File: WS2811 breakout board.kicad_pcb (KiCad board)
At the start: 2 copper layers, 25.4 x 17.8 mm, 15 parts

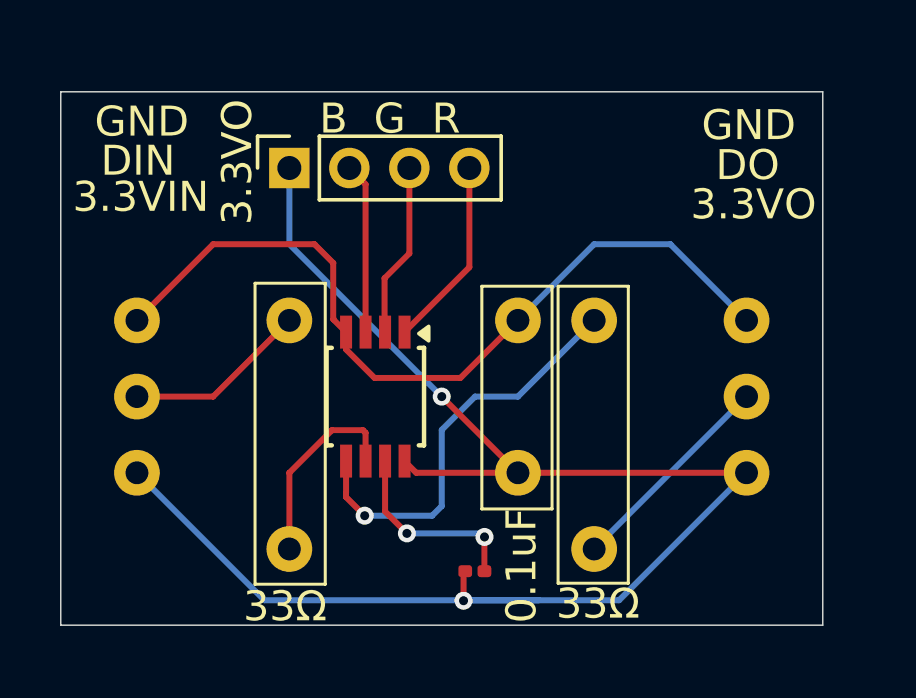
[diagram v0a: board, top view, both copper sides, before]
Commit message: fix sizing issues
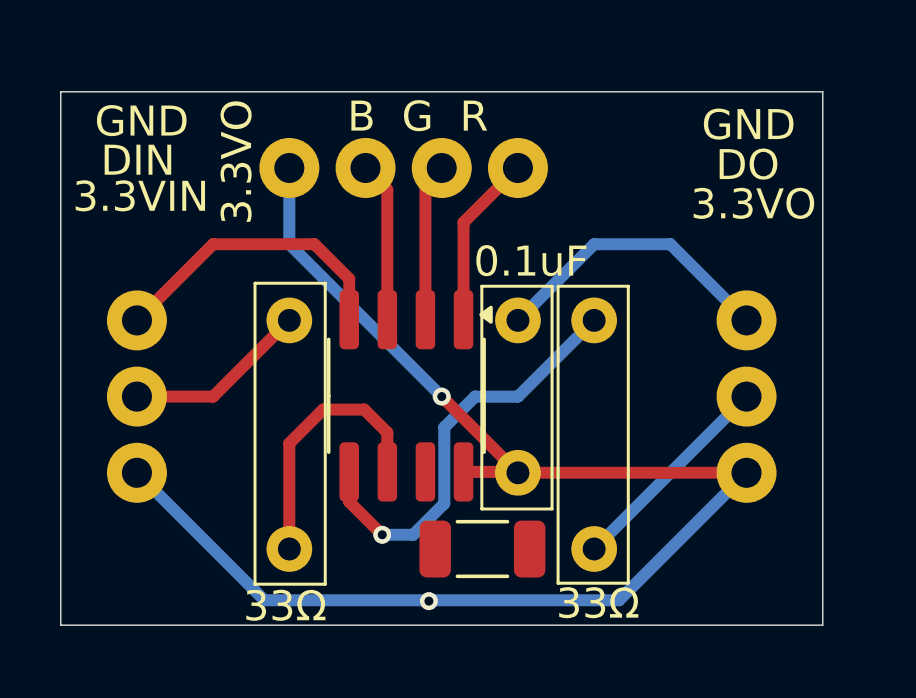
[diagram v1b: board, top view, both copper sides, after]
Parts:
- removed the REF** at (148.4, 92.2)
- removed the REF** at (145.1, 86.4)
- removed the REF** at (142.2, 78.7)
- added ?: , , F.Cu at (142.2, 78.7)
- added ?: , , F.Cu at (144.8, 78.7)
- added ?: , , F.Cu at (149.9, 78.7)
- added ?: , , F.Cu at (147.3, 78.7)
- added REF**: SOP-8_3.76x4.96mm_P1.27mm, Package_SO:SOP-8_3.76x4.96mm_P1.27mm, F.Cu at (146.1, 86.3)
- added REF**: L_1206_3216Metric, Inductor_SMD:L_1206_3216Metric, F.Cu at (148.7, 91.4)
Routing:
- net (no net): track 138.1 -> 119.2 mm, vias 5 -> 3

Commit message: fix missing trace
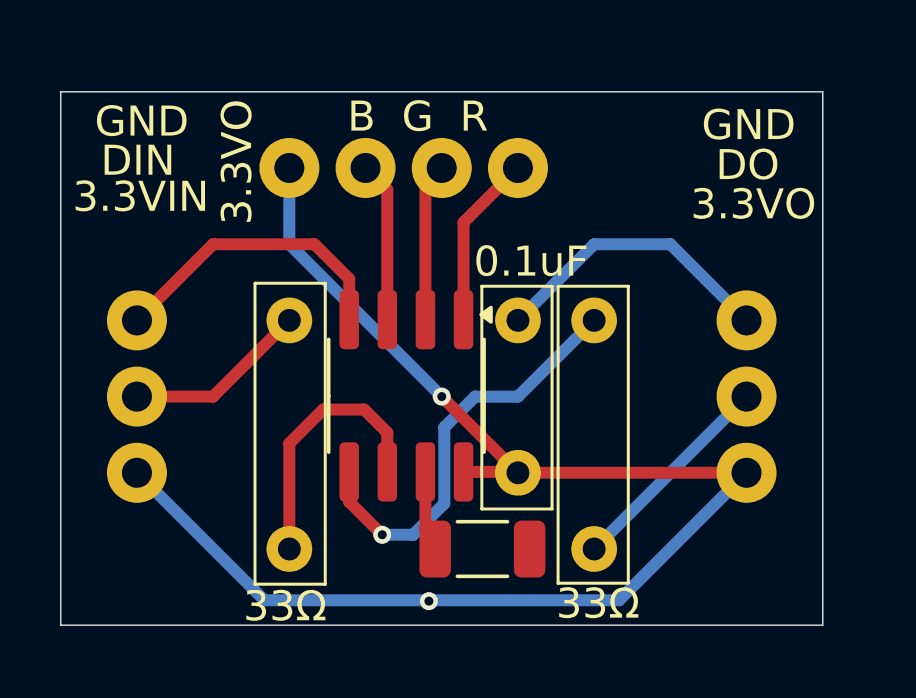
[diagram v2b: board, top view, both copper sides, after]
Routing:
- net (no net): track 119.2 -> 121.8 mm
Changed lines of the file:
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@@
+	)
+	(segment
+		(start 147.101123 91.144977)
+		(end 147.101123 91.440946)
+		(width 0.4)
+		(layer "F.Cu")
+		(net 0)
 	)
 	(segment
@@
 	)
 	(segment
+		(start 146.776604 88.870747)
+		(end 146.776604 90.820458)
+		(width 0.4)
+		(layer "F.Cu")
+		(net 0)
+	)
+	(segment
 		(start 142.24 87.917865)
 		(end 143.366776 86.791089)
@@
 		(end 148.046604 80.553396)
 		(width 0.4)
-		(layer "F.Cu")
-		(net 0)
-	)
-	(segment
-		(start 146.870338 88.964481)
-		(end 146.776604 88.870747)
-		(width 0.2)
 		(layer "F.Cu")
 		(net 0)
@@
 		(width 0.4)
 		(layer "F.Cu")
+		(net 0)
+	)
+	(segment
+		(start 146.776604 90.820458)
+		(end 147.101123 91.144977)
+		(width 0.4)
+		(layer "F.Cu")

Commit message: fix another missing trace
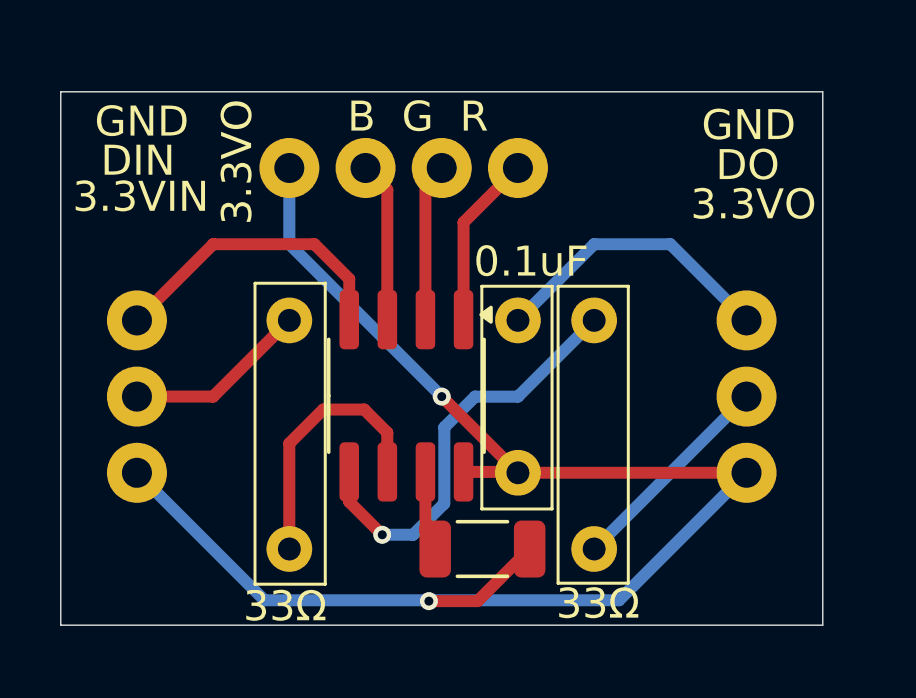
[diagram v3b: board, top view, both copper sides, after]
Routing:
- net (no net): track 121.8 -> 125.8 mm
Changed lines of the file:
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@@
+	)
+	(segment
+		(start 148.513374 93.178695)
+		(end 146.89175 93.178695)
+		(width 0.4)
+		(layer "F.Cu")
+		(net 0)
+	)
+	(segment
+		(start 150.251123 91.440946)
+		(end 148.513374 93.178695)
+		(width 0.4)
+		(layer "F.Cu")
+		(net 0)
 	)
 	(segment

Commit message: update board to v2.5
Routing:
- net (no net): track 125.8 -> 115.0 mm, vias 3 -> 0
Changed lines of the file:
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@@
 	)
 	(segment
-		(start 144.737175 86.791089)
-		(end 145.506604 87.560518)
+		(start 149.86 93.238647)
+		(end 141.498647 93.238647)
+		(width 0.4)
+		(layer "F.Cu")
+		(net 0)
+	)
+	(segment
+		(start 139.033372 78.74)
+		(end 142.24 78.74)
+		(width 0.4)
+		(layer "F.Cu")
+		(net 0)
+	)
+	(segment
+		(start 141.498647 93.238647)
+		(end 137.16 88.9)
+		(width 0.4)
+		(layer "F.Cu")
+		(net 0)
+	)
+	(segment
+		(start 153.141353 93.238647)
+		(end 149.86 93.238647)
 		(width 0.4)
 		(layer "F.Cu")
@@
 	)
 	(segment
-		(start 145.506604 87.560518)
-		(end 145.506604 88.870747)
-		(width 0.4)
-		(layer "F.Cu")
-		(net 0)
-	)
-	(segment
 		(start 147.101123 91.144977)
 		(end 147.101123 91.440946)
@@
 	)
 	(segment
+		(start 144.236604 88.870747)
+		(end 144.236604 86.903396)
+		(width 0.4)
+		(layer "F.Cu")
+		(net 0)
+	)
+	(segment
 		(start 148.046604 80.553396)
 		(end 149.86 78.74)
@@
 	)
 	(segment
-		(start 146.870338 93.157283)
-		(end 146.89175 93.178695)
-		(width 0.4)
-		(layer "F.Cu")
-		(net 0)
-	)
-	(segment
-		(start 144.236604 88.870747)
-		(end 144.236604 89.866401)
+		(start 150.251123 91.440946)
+		(end 150.251123 89.291123)
+		(width 0.4)
+		(layer "F.Cu")
+		(net 0)
+	)
+	(segment
+		(start 145.506604 90.713396)
+		(end 144.78 91.44)
 		(width 0.4)
 		(layer "F.Cu")
@@
 	)
 	(segment
+		(start 135.329233 87.069233)
+		(end 135.329233 82.444139)
+		(width 0.4)
+		(layer "F.Cu")
+		(net 0)
+	)
+	(segment
 		(start 137.16 86.36)
 		(end 139.7 86.36)
@@
 	)
 	(segment
-		(start 149.86 88.9)
-		(end 157.48 88.9)
+		(start 144.78 91.44)
+		(end 142.24 91.44)
 		(width 0.4)
 		(layer "F.Cu")
@@
 	)
 	(segment
-		(start 142.24 91.44)
-		(end 142.24 87.917865)
+		(start 135.329233 82.444139)
+		(end 139.033372 78.74)
+		(width 0.4)
+		(layer "F.Cu")
+		(net 0)
+	)
+	(segment
+		(start 152.4 81.28)
+		(end 154.94 81.28)
+		(width 0.4)
+		(layer "F.Cu")
+		(net 0)
+	)
+	(segment
+		(start 145.506604 88.870747)
+		(end 145.506604 90.713396)
 		(width 0.4)
 		(layer "F.Cu")
@@
 	)
 	(segment
+		(start 150.251123 89.291123)
+		(end 149.86 88.9)
+		(width 0.4)
+		(layer "F.Cu")
+		(net 0)
+	)
+	(segment
+		(start 150.251123 92.847524)
+		(end 149.86 93.238647)
+		(width 0.4)
+		(layer "F.Cu")
+		(net 0)
+	)
+	(segment
 		(start 146.776604 79.283396)
 		(end 147.32 78.74)
@@
 	)
 	(segment
-		(start 142.24 87.917865)
-		(end 143.366776 86.791089)
+		(start 137.16 88.9)
+		(end 135.329233 87.069233)
+		(width 0.4)
+		(layer "F.Cu")
+		(net 0)
+	)
+	(segment
+		(start 144.78 86.36)
+		(end 149.86 86.36)
+		(width 0.4)
+		(layer "F.Cu")
+		(net 0)
+	)
+	(segment
+		(start 152.4 91.44)
+		(end 157.48 86.36)
+		(width 0.4)
+		(layer "F.Cu")
+		(net 0)
+	)
+	(segment
+		(start 149.86 83.82)
+		(end 152.4 81.28)
 		(width 0.4)
 		(layer "F.Cu")
@@
 	)
 	(segment
-		(start 143.366776 86.791089)
-		(end 144.737175 86.791089)
-		(width 0.4)
-		(layer "F.Cu")
-		(net 0)
-	)
-	(segment
-		(start 149.86 88.9)
-		(end 147.32 86.36)
-		(width 0.4)
-		(layer "F.Cu")
-		(net 0)
-	)
-	(segment
-		(start 148.513374 93.178695)
-		(end 146.89175 93.178695)
+		(start 149.86 86.36)
+		(end 152.4 83.82)
 		(width 0.4)
 		(layer "F.Cu")
@@
 	(segment
 		(start 150.251123 91.440946)
-		(end 148.513374 93.178695)
+		(end 150.251123 92.847524)
+		(width 0.4)
+		(layer "F.Cu")
+		(net 0)
+	)
+	(segment
+		(start 144.236604 86.903396)
+		(end 144.78 86.36)
+		(width 0.4)
+		(layer "F.Cu")
+		(net 0)
+	)
+	(segment
+		(start 154.94 81.28)
+		(end 157.48 83.82)
 		(width 0.4)
 		(layer "F.Cu")
@@
 	)
 	(segment
+		(start 157.48 88.9)
+		(end 153.141353 93.238647)
+		(width 0.4)
+		(layer "F.Cu")
+		(net 0)
+	)
+	(segment
 		(start 149.830747 88.870747)
 		(end 149.86 88.9)
@@
 		(net 0)
 	)
-	(segment
-		(start 144.236604 89.866401)
-		(end 145.336724 90.966521)
-		(width 0.4)
-		(layer "F.Cu")
-		(net 0)
-	)
-	(via
-		(at 145.336724 90.966521)
-		(size 0.6)
-		(drill 0.3)
-		(layers "F.Cu" "B.Cu")
-		(net 0)
-	)
-	(via
-		(at 147.32 86.36)
-		(size 0.6)
-		(drill 0.3)
-		(layers "F.Cu" "B.Cu")
-		(net 0)
-	)
-	(via
-		(at 146.89175 93.178695)
-		(size 0.6)
-		(drill 0.3)
-		(layers "F.Cu" "B.Cu")
-		(net 0)
-	)
-	(segment
-		(start 146.921399 93.149046)
-		(end 153.230954 93.149046)
-		(width 0.4)
-		(layer "B.Cu")
-		(net 0)
-	)
-	(segment
-		(start 147.405649 87.384001)
-		(end 148.42965 86.36)
-		(width 0.4)
-		(layer "B.Cu")
-		(net 0)
-	)
-	(segment
-		(start 152.4 81.28)
-		(end 154.94 81.28)
-		(width 0.4)
-		(layer "B.Cu")
-		(net 0)
-	)
-	(segment
-		(start 141.409046 93.149046)
-		(end 146.862101 93.149046)
-		(width 0.4)
-		(layer "B.Cu")
-		(net 0)
-	)
-	(segment
-		(start 149.86 83.82)
-		(end 152.4 81.28)
-		(width 0.4)
-		(layer "B.Cu")
-		(net 0)
-	)
-	(segment
-		(start 153.230954 93.149046)
-		(end 157.48 88.9)
-		(width 0.4)
-		(layer "B.Cu")
-		(net 0)
-	)
-	(segment
-		(start 142.24 81.28)
-		(end 142.24 78.74)
-		(width 0.4)
-		(layer "B.Cu")
-		(net 0)
-	)
-	(segment
-		(start 147.32 86.36)
-		(end 142.24 81.28)
-		(width 0.4)
-		(layer "B.Cu")
-		(net 0)
-	)
-	(segment
-		(start 146.862101 93.149046)
-		(end 146.89175 93.178695)
-		(width 0.4)
-		(layer "B.Cu")
-		(net 0)
-	)
-	(segment
-		(start 152.4 91.44)
-		(end 157.48 86.36)
-		(width 0.4)
-		(layer "B.Cu")
-		(net 0)
-	)
-	(segment
-		(start 147.405649 89.924001)
-		(end 147.405649 87.384001)
-		(width 0.4)
-		(layer "B.Cu")
-		(net 0)
-	)
-	(segment
-		(start 154.94 81.28)
-		(end 157.48 83.82)
-		(width 0.4)
-		(layer "B.Cu")
-		(net 0)
-	)
-	(segment
-		(start 145.336724 90.966521)
-		(end 146.363129 90.966521)
-		(width 0.4)
-		(layer "B.Cu")
-		(net 0)
-	)
-	(segment
-		(start 146.89175 93.178695)
-		(end 146.921399 93.149046)
-		(width 0.4)
-		(layer "B.Cu")
-		(net 0)
-	)
-	(segment
-		(start 148.42965 86.36)
-		(end 149.86 86.36)
-		(width 0.4)
-		(layer "B.Cu")
-		(net 0)
-	)
-	(segment
-		(start 146.363129 90.966521)
-		(end 147.405649 89.924001)
-		(width 0.4)
-		(layer "B.Cu")
-		(net 0)
-	)
-	(segment
-		(start 149.86 86.36)
-		(end 152.4 83.82)
-		(width 0.4)
-		(layer "B.Cu")
-		(net 0)
-	)
-	(segment
-		(start 137.16 88.9)
-		(end 141.409046 93.149046)
-		(width 0.4)
-		(layer "B.Cu")
-		(net 0)
-	)

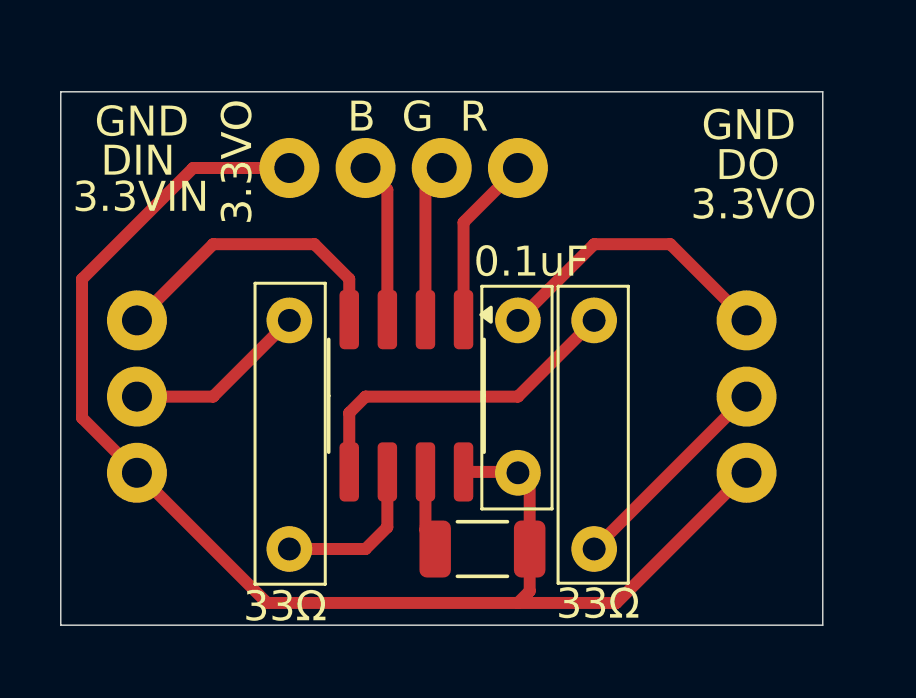
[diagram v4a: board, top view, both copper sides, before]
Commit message: fix gnd trace disconnect
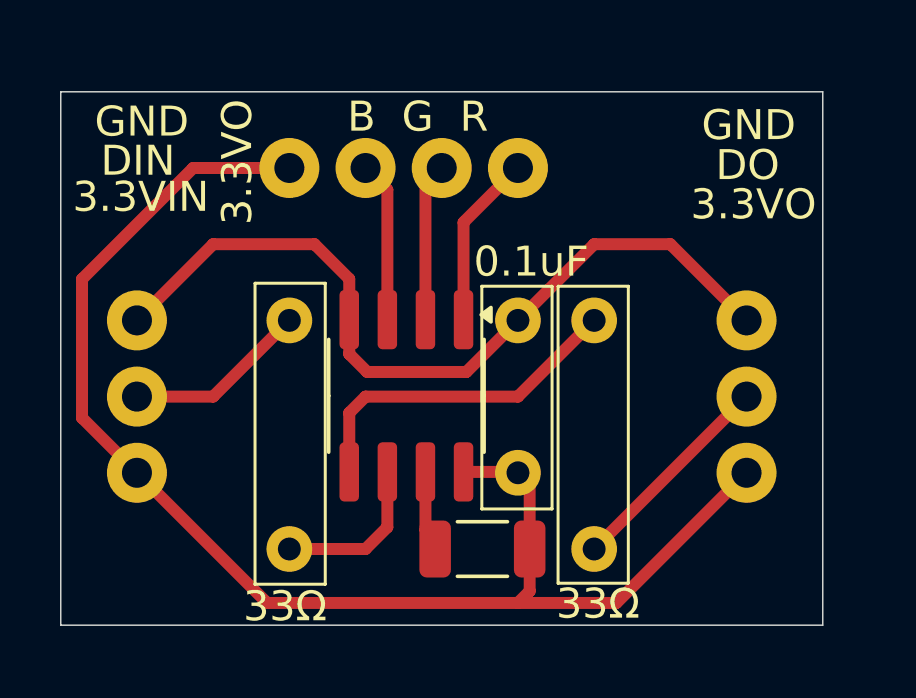
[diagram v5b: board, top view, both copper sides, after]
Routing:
- net (no net): track 115.0 -> 122.8 mm
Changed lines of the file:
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@@
+	)
+	(segment
+		(start 144.836152 85.539661)
+		(end 144.236604 84.940113)
+		(width 0.4)
+		(layer "F.Cu")
+		(net 0)
 	)
 	(segment
@@
 	)
 	(segment
+		(start 148.140339 85.539661)
+		(end 144.836152 85.539661)
+		(width 0.4)
+		(layer "F.Cu")
+		(net 0)
+	)
+	(segment
+		(start 149.86 83.82)
+		(end 148.140339 85.539661)
+		(width 0.4)
+		(layer "F.Cu")
+		(net 0)
+	)
+	(segment
 		(start 149.86 83.82)
 		(end 152.4 81.28)
 		(width 0.4)
 		(layer "F.Cu")
+		(net 0)
+	)
+	(segment
+		(start 144.236604 84.940113)
+		(end 144.236604 83.795747)
+		(width 0.4)
+		(layer "F.Cu")
